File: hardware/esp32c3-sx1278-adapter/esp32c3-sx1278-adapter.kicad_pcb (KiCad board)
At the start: 2 copper layers, 24 x 58 mm, 5 parts, among them J1 Conn_01x08, J2 Conn_01x08, J3 Antenna, J4 SMA, U2 SX1278_module

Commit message: Adapters: expansion header for the unused SuperMini pins and a radio-type strap
Pin-header adapter:
* J4, a 1x7 2.54 mm header on the top edge, carries every SuperMini pin the
  radio does not use: 5V, GPIO8, GPIO9, GPIO2, GPIO20, GPIO21, GPIO0.  Its
  pins sit at the gaps between the SuperMini's pins so each net reaches it on
  the front copper without crossing another (power-row nets jog above their
  row, GPIO-row nets rise between the rows and pass between the power-row
  pads).  The radio tracks on the back are unchanged; the GND pour flows
  around the new tracks.
* JP1, a two-pad solder jumper right of the SuperMini, straps GPIO1 (net
  RADIO_ID) to GND: open = CC1101 E07-M1101D, bridged = Ra-02 breakout.

SX1278 module adapter: GPIO1 is tied to 3V3 (silk "ID=3V3"), so the same
pin reads high there.  Firmware samples GPIO1 with the internal pull-down
and then the pull-up to tell the three states apart; GPIO1 is not a boot
strapping pin.

The header is 2.3 mm from the top edge so the MISO lane on the back keeps
its clearance under it.  Both adapters pass ERC and DRC; README and the
manufacturing notes describe the header and the strap.

Co-Authored-By: Claude Fable 5.1 <noreply@anthropic.com>
Claude-Session: https://claude.ai/code/session_01JoGdh4Cg3VtTTDZi4gQuiN
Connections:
- J2 pad 7: GPIO1 -> +3V3
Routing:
- net +3V3: track 28.2 -> 41.0 mm
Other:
- board text added: "ID=3V3"
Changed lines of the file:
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@@
 	(net 13 "DIO1")
 	(net 14 "GPIO2")
-	(net 15 "GPIO1")
-	(net 16 "GPIO0")
-	(net 17 "DIO2")
-	(net 18 "DIO3")
-	(net 19 "DIO4")
-	(net 20 "DIO5")
-	(net 21 "ANT")
+	(net 15 "GPIO0")
+	(net 16 "DIO2")
+	(net 17 "DIO3")
+	(net 18 "DIO4")
+	(net 19 "DIO5")
+	(net 20 "ANT")
 	(footprint "Adapter:SuperMini_Header_1x08_P2.54mm_THT"
 		(layer "F.Cu")
@@
 			(layers "*.Cu" "*.Mask")
 			(remove_unused_layers no)
-			(net 15 "GPIO1")
+			(net 11 "+3V3")
 			(pinfunction "Pin_7")
 			(pintype "passive")
@@
 			(layers "*.Cu" "*.Mask")
 			(remove_unused_layers no)
-			(net 16 "GPIO0")
+			(net 15 "GPIO0")
 			(pinfunction "Pin_8")
 			(pintype "passive")
@@
 			(size 1 3)
 			(layers "F.Cu" "F.Mask" "F.Paste")
-			(net 17 "DIO2")
+			(net 16 "DIO2")
 			(pinfunction "Pin_3")
 			(pintype "passive")
@@
 			(size 1 3)
 			(layers "F.Cu" "F.Mask" "F.Paste")
-			(net 18 "DIO3")
+			(net 17 "DIO3")
 			(pinfunction "Pin_4")
 			(pintype "passive")
@@
 			(size 2 0.8)
 			(layers "F.Cu" "F.Mask" "F.Paste")
-			(net 19 "DIO4")
+			(net 18 "DIO4")
 			(pinfunction "Pin_13")
 			(pintype "passive")
@@
 			(size 2 0.8)
 			(layers "F.Cu" "F.Mask" "F.Paste")
-			(net 20 "DIO5")
+			(net 19 "DIO5")
 			(pinfunction "Pin_14")
 			(pintype "passive")
@@
 			(size 1 3)
 			(layers "F.Cu" "F.Mask" "F.Paste")
-			(net 21 "ANT")
+			(net 20 "ANT")
 			(pinfunction "Pin_16")
 			(pintype "passive")
@@
 			(layers "*.Cu" "*.Mask")
 			(remove_unused_layers no)
-			(net 21 "ANT")
+			(net 20 "ANT")
 			(pinfunction "Pin_1")
 			(pintype "passive")
@@
 			(size 1.5 4.5)
 			(layers "F.Cu" "F.Mask" "F.Paste")
-			(net 21 "ANT")
+			(net 20 "ANT")
 			(pinfunction "Pin_1")
 			(pintype "passive")
@@
 		)
 	)
+	(gr_text "ID=3V3"
+		(at 118.04 119.24 0)
+		(layer "F.SilkS")
+		(effects
+			(font
+				(size 0.6 0.6)
+				(thickness 0.09)
+			)
+			(justify right)
+		)
+	)
 	(gr_text "0"
 		(at 120.44 121.78 0)
@@
 		(layer "F.Cu")
 		(net 13)
+	)
+	(segment
+		(start 119.24 109.08)
+		(end 120.54 109.08)
+		(width 0.25)
+		(layer "F.Cu")
+		(net 11)
+	)
+	(segment
+		(start 120.54 109.08)
+		(end 120.54 119.24)
+		(width 0.25)
+		(layer "F.Cu")
+		(net 11)
+	)
+	(segment
+		(start 120.54 119.24)
+		(end 119.24 119.24)
+		(width 0.25)
+		(layer "F.Cu")
+		(net 11)
 	)
 	(segment
@@
 		(width 0.5)
 		(layer "F.Cu")
-		(net 21)
+		(net 20)
 	)
 	(segment
@@
 		(width 0.5)
 		(layer "F.Cu")
-		(net 21)
+		(net 20)
 	)
 	(segment
@@
 		(width 0.5)
 		(layer "F.Cu")
-		(net 21)
-	)
-	(segment
+		(net 20)
+	)
+	(segment

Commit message: Adapters: reassign the GPIOs so the socket adapter routes on one layer
The pin-header (socket) adapter is now entirely on the back copper, the
expansion header and strap included; the front carries only pads and the
GND pour.  New assignment, shared by both adapters:

  MOSI GPIO8, SCK GPIO9, CSN/NSS GPIO0, MISO GPIO7, GDO0/RST(DIO0) GPIO10,
  GDO2/DIO0(DIO1) GPIO6, strap RADIO_ID GPIO5, SX1278 module RESET GPIO4.

GPIO8/9 are boot strapping pins but carry only ESP32 outputs, which float
at boot; the radio's outputs stay on plain GPIOs.  On the socket adapter
the radio signals then all leave the GPIO row, which faces the socket, in
the order its pads want them: GDO0 and SCK drop straight in, MOSI and MISO
via one lane each, GDO2 round the left of the socket into its pad from
below.  CSN/NSS (GPIO0, the last power-row pin) passes under its own pad,
crosses between the rows (now otherwise empty) and drops through a
GPIO-row gap.  GND and 3V3 leave the power row upward, run along the top
edge above the header and down the strip right of the SuperMini into the
socket's right column; GND continues under the socket to the strap.

Expansion header J4 (centred): 3V3, GPIO4, 3, 2, 1, 21, 20 - GPIO4..1 rise
straight up, GPIO21/20 come up the right-hand strip.  5V is dropped: its
pad sits under the top-left hole and cannot be reached on one layer.  The
strap moves to the bottom-left corner (JP1 header, R1 0805 on the back),
fed by GPIO5 dropping straight down and by the under-socket GND lane.

SX1278 module adapter: same map; its GPIO order matches the module's pad
order so the front-copper lanes stay nested; NSS and RESET now come from
the right column on the back copper, 3V3 goes down the right of the
SuperMini, and GPIO5 is tied to 3V3 across the top.

Both adapters pass ERC and DRC; the antenna keepout starts 1.6 mm inboard
of the power row (was 1.3) to give CSN/NSS its lane under the last pad.

Co-Authored-By: Claude Fable 5.1 <noreply@anthropic.com>
Claude-Session: https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
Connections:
- J1 pad 1: MOSI -> +3V3
- J1 pad 2: SCK -> DIO1
- J1 pad 3: NSS -> MISO
- J1 pad 4: RESET -> MOSI
- J1 pad 5: GPIO9 -> SCK
- J2 pad 4: MISO -> RESET
- J2 pad 5: DIO1 -> GPIO3
- J2 pad 7: +3V3 -> GPIO1
- J2 pad 8: GPIO0 -> NSS
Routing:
- net DIO1: track 19.3 -> 39.2 mm
- net RESET: track 22.7 -> 33.3 mm
- net +3V3: track 41.0 -> 51.2 mm
- net MOSI: track 35.4 -> 27.8 mm
- net SCK: track 31.6 -> 24.0 mm
- net NSS: track 27.8 -> 20.6 mm, vias 0 -> 1
- net MISO: track 26.9 -> 31.6 mm

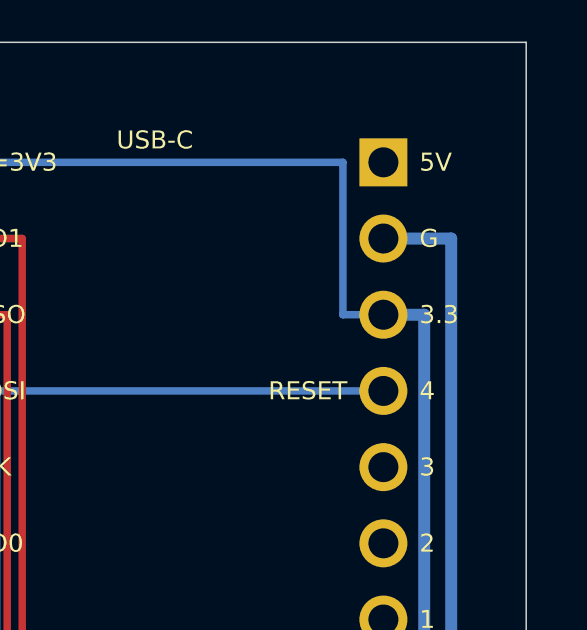
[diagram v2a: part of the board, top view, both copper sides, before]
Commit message: Silk: "3V3" instead of "3.3", and the UART pins named on the spare header
The 3.3 V pin is labelled 3V3 on the SuperMini board and beside the
SuperMini on the adapters, and the expansion header's GPIO21/20 pins read
"21TX" / "20RX".

Co-Authored-By: Claude Fable 5.1 <noreply@anthropic.com>
Claude-Session: https://claude.ai/code/session_01JoGdh4Cg3VtTTDZi4gQuiN
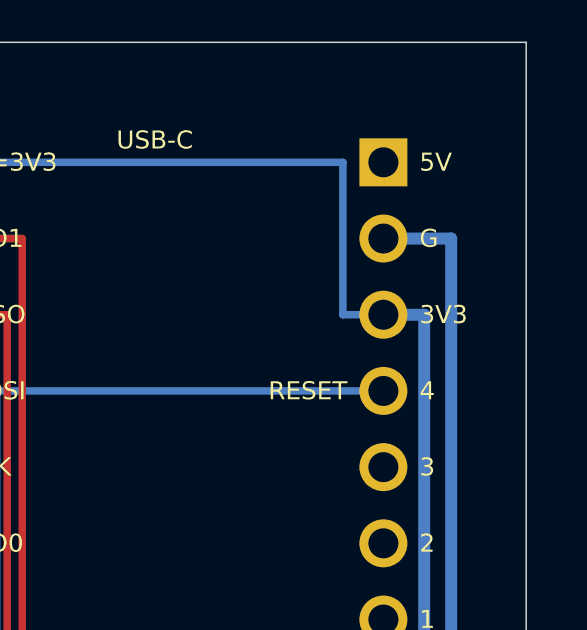
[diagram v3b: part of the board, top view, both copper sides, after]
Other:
- board text added: "3V3"
- board text removed: "3.3"
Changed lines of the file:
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@@
 		)
 	)
-	(gr_text "3.3"
+	(gr_text "3V3"
 		(at 120.44 109.08 0)
 		(layer "F.SilkS")
